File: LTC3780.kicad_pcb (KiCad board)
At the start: 2 copper layers, 46 parts, among them Q2 IPD100N04S402ATMA1, Q3 IPD100N04S402ATMA1, Q4 IPD100N04S402ATMA1, Q5 IPD100N04S402ATMA1, U1 LTC3780EGPBF

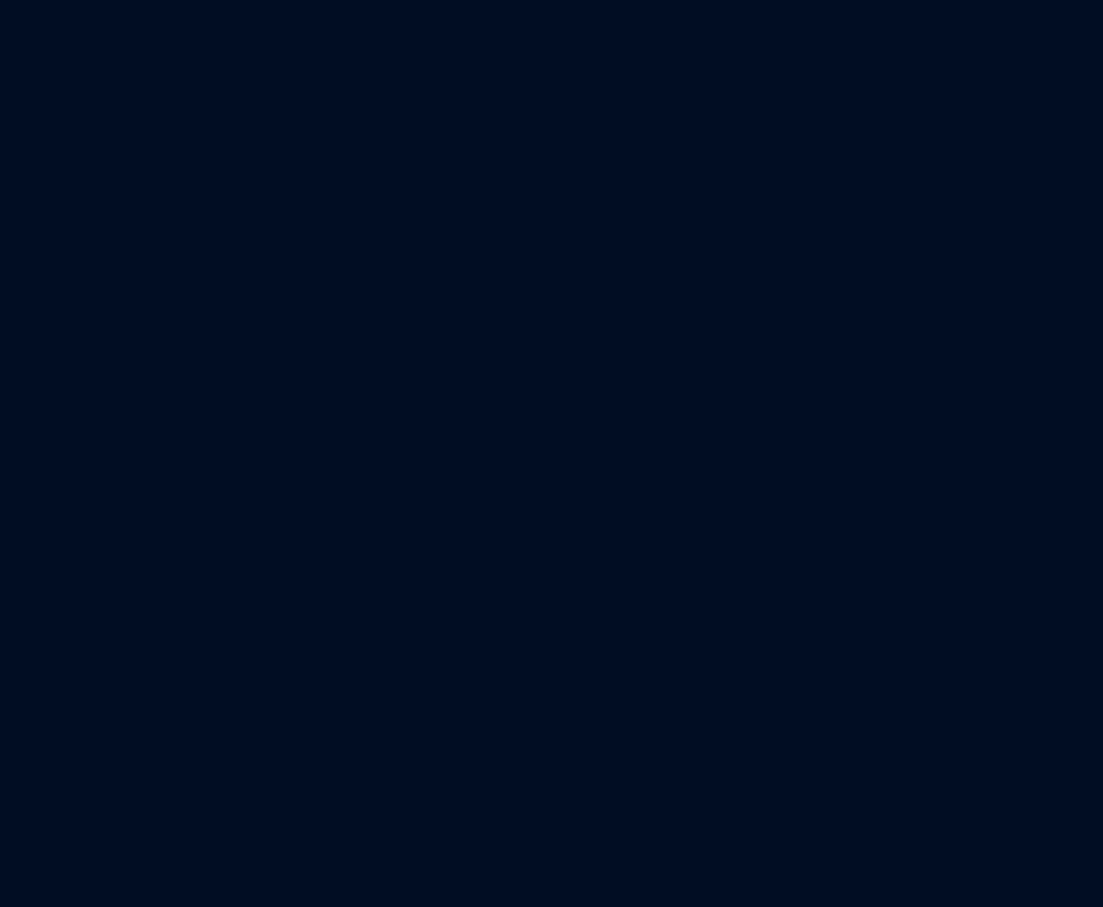
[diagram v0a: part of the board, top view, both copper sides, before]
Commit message: Updated PCB from Netlist
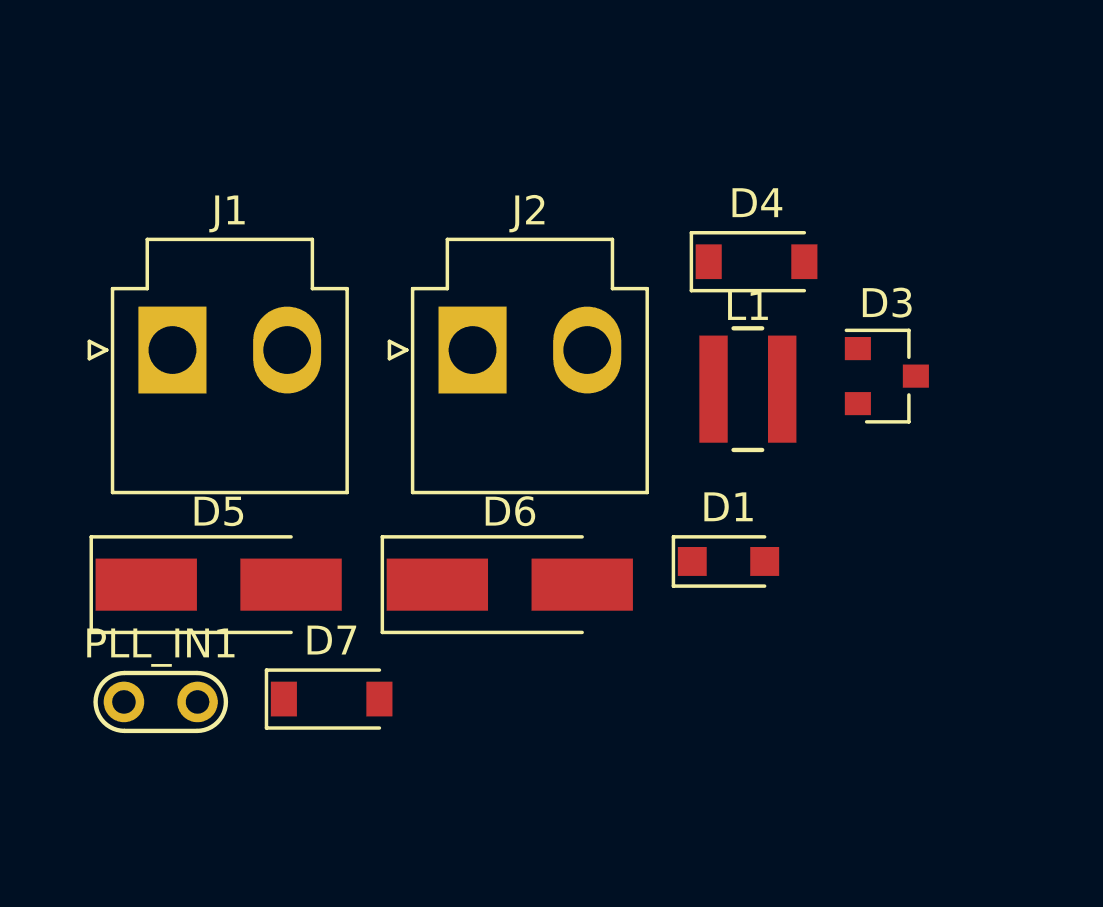
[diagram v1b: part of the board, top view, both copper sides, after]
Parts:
- added D1: 4.7V, Diodes_SMD:D_SOD-323_HandSoldering, F.Cu at (150.0, 89.3)
- added D3: 36V, Diodes_SMD:D_SOT-23_ANK, F.Cu at (155.5, 82.9)
- added D4: 1N819HW, Diodes_SMD:D_SOD-123, F.Cu at (151.0, 78.9)
- added D5: B320A, Diodes_SMD:D_SMA_Handsoldering, F.Cu at (132.4, 90.1)
- added D6: B320A, Diodes_SMD:D_SMA_Handsoldering, F.Cu at (142.5, 90.1)
- added D7: 1N819HW, Diodes_SMD:D_SOD-123, F.Cu at (136.3, 94.0)
- added J1: Screw_Terminal_01x02, Connectors_JST:JST_VH_B2P-VH_2x3.96mm_Vertical, F.Cu at (130.8, 82.0)
- added J2: Screw_Terminal_01x02, Connectors_JST:JST_VH_B2P-VH_2x3.96mm_Vertical, F.Cu at (141.2, 82.0)
- added L1: 4.7uH, Inductors:Inductor_Wurth_MAPI-4020, F.Cu at (150.7, 83.3)
- added PLL_IN1: TestPoint, Measurement_Points:Test_Point, F.Cu at (129.1, 94.1)

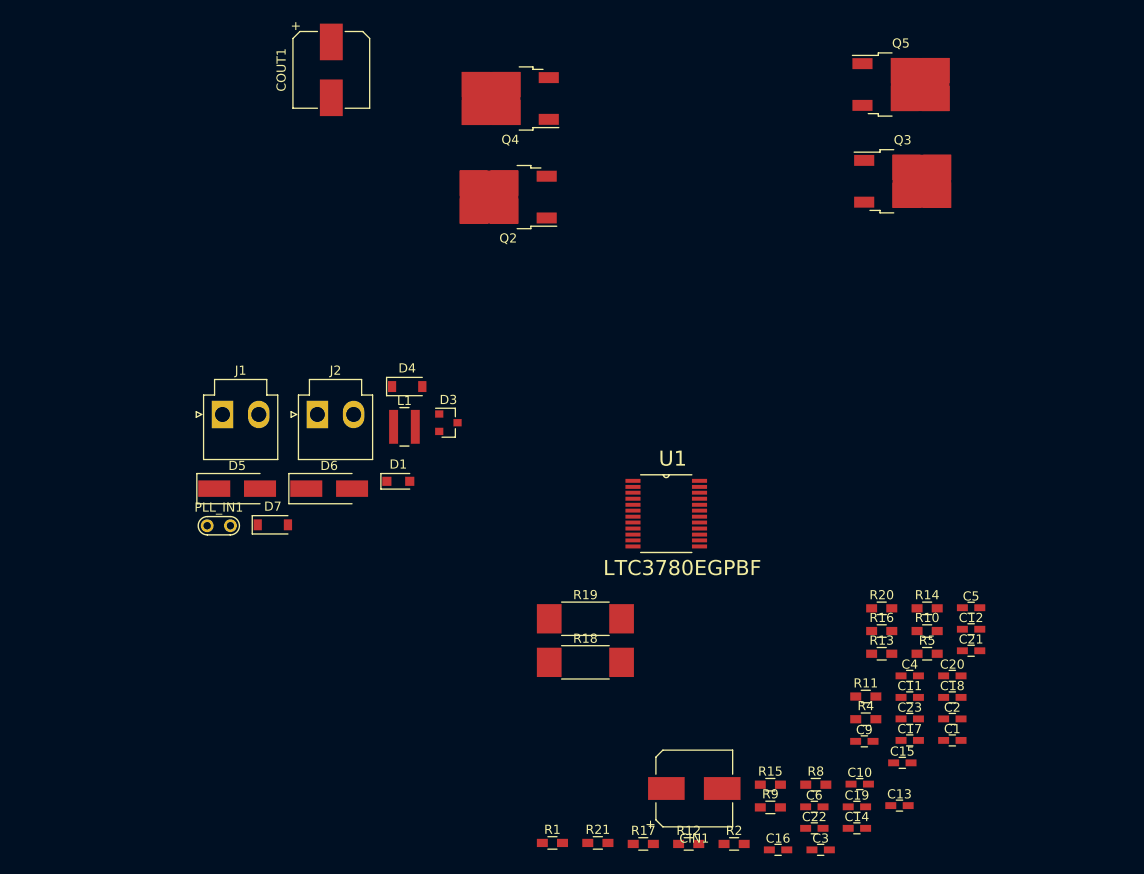
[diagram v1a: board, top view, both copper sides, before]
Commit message: Updated with drawing dimensions for board
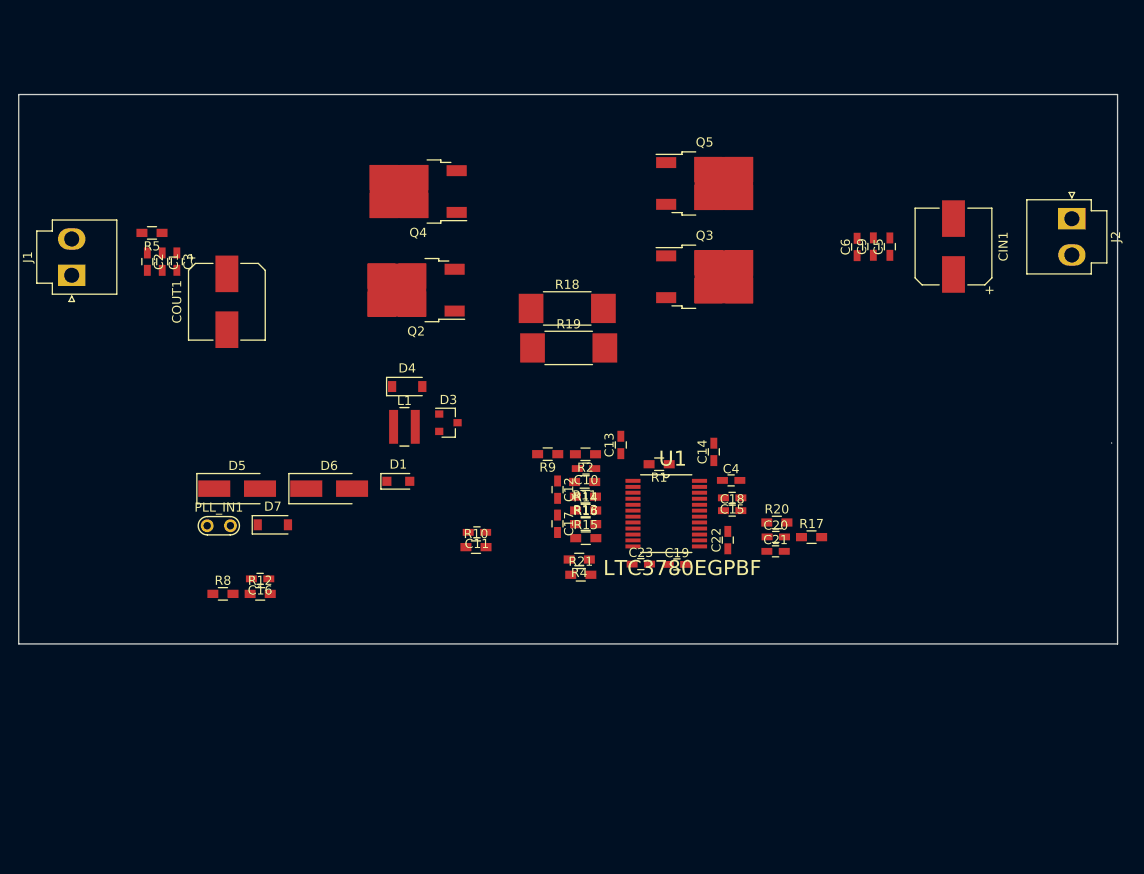
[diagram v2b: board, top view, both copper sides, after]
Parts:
- moved C2 101.1 mm to (122.6, 65.3), turned to 270 degrees
- moved C1 100.9 mm to (124.2, 65.3), turned to 270 degrees
- moved R5 96.3 mm to (123.1, 62.1), turned to 180 degrees
- moved C3 95.2 mm to (125.8, 65.3), turned to 270 degrees
- moved J2 85.1 mm to (223.6, 60.6), turned to 270 degrees
- moved R8 68.0 mm to (130.9, 101.5)
- moved CIN1 65.6 mm to (210.6, 63.6), turned to 90 degrees
- moved C16 63.8 mm to (134.9, 99.9), turned to 180 degrees
- moved C6 61.3 mm to (200.1, 63.7), turned to 90 degrees
- moved R12 54.2 mm to (134.9, 101.5)
- moved C9 54.0 mm to (201.9, 63.6), turned to 90 degrees
- moved C11 50.6 mm to (158.6, 94.8), turned to 180 degrees
- moved R10 50.1 mm to (158.5, 96.4)
- moved C13 49.8 mm to (174.3, 85.3), turned to 90 degrees
- moved C12 47.7 mm to (167.4, 90.2), turned to 270 degrees
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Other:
- board outline added: 120 x 60 mm

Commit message: Routed and placed some components
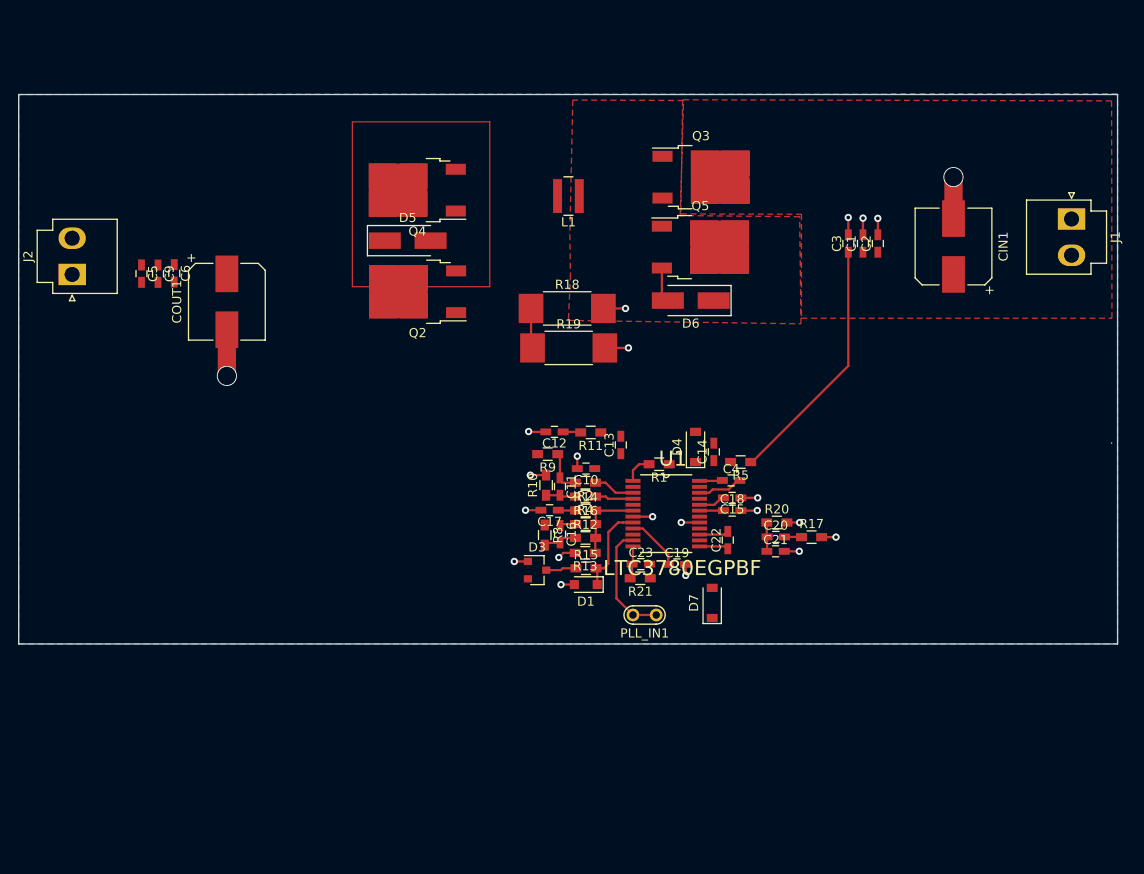
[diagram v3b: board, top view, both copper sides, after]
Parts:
- moved J1 109.4 mm to (223.5, 60.6), turned to 270 degrees
- moved J2 109.3 mm to (114.4, 66.7), turned to 90 degrees
- moved C5 81.8 mm to (122.0, 66.6), turned to 270 degrees
- moved C2 79.8 mm to (202.4, 63.3), turned to 90 degrees
- moved C9 78.2 mm to (123.8, 66.6), turned to 270 degrees
- moved C1 76.6 mm to (200.8, 63.3), turned to 90 degrees
- moved C6 74.6 mm to (125.5, 66.5), turned to 270 degrees
- moved C3 73.4 mm to (199.2, 63.3), turned to 90 degrees
- moved R5 69.0 mm to (187.4, 87.2)
- moved PLL_IN1 50.0 mm to (178.2, 103.9), turned to 180 degrees
- moved D7 48.7 mm to (184.3, 102.5), turned to 90 degrees
- moved D6 44.5 mm to (182.0, 69.5), turned to 180 degrees
- moved R12 36.0 mm to (170.5, 95.4)
- moved R8 35.7 mm to (166.0, 95.1), turned to 270 degrees
- moved C16 33.1 mm to (167.7, 95.0), turned to 270 degrees
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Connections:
- U1 pad 11: (no net) -> Net-(PLL_IN1-Pad1)
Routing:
- net GND: track 0.00 -> 45.3 mm, vias 0 -> 22
- net +VSW: track 0.00 -> 30.7 mm
- net Net-(PLL_IN1-Pad1): track 0.00 -> 12.8 mm
- net Net-(D1-Pad1): track 0.00 -> 9.95 mm
- net VSENSE: track 0.00 -> 8.71 mm
- net Net-(D6-Pad2): track 0.00 -> 8.21 mm
- net Net-(C19-Pad1): track 0.00 -> 6.14 mm
- net SW1: track 0.00 -> 4.96 mm
- net Net-(C11-Pad1): track 0.00 -> 4.74 mm
- net SENSE+: track 0.00 -> 4.55 mm
- net SENSE-: track 0.00 -> 4.19 mm
- net Net-(C16-Pad2): track 0.00 -> 3.80 mm
- net Net-(C23-Pad1): track 0.00 -> 3.60 mm
- net Net-(C11-Pad2): track 0.00 -> 3.26 mm
- net SW2: track 0.00 -> 3.23 mm
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- added copper zone on F.Cu, net +VSW
- added copper zone on B.Cu, net GND
- added copper zone on F.Cu, net SW2

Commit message: Finished PCB first layout and routing, generated gerber files
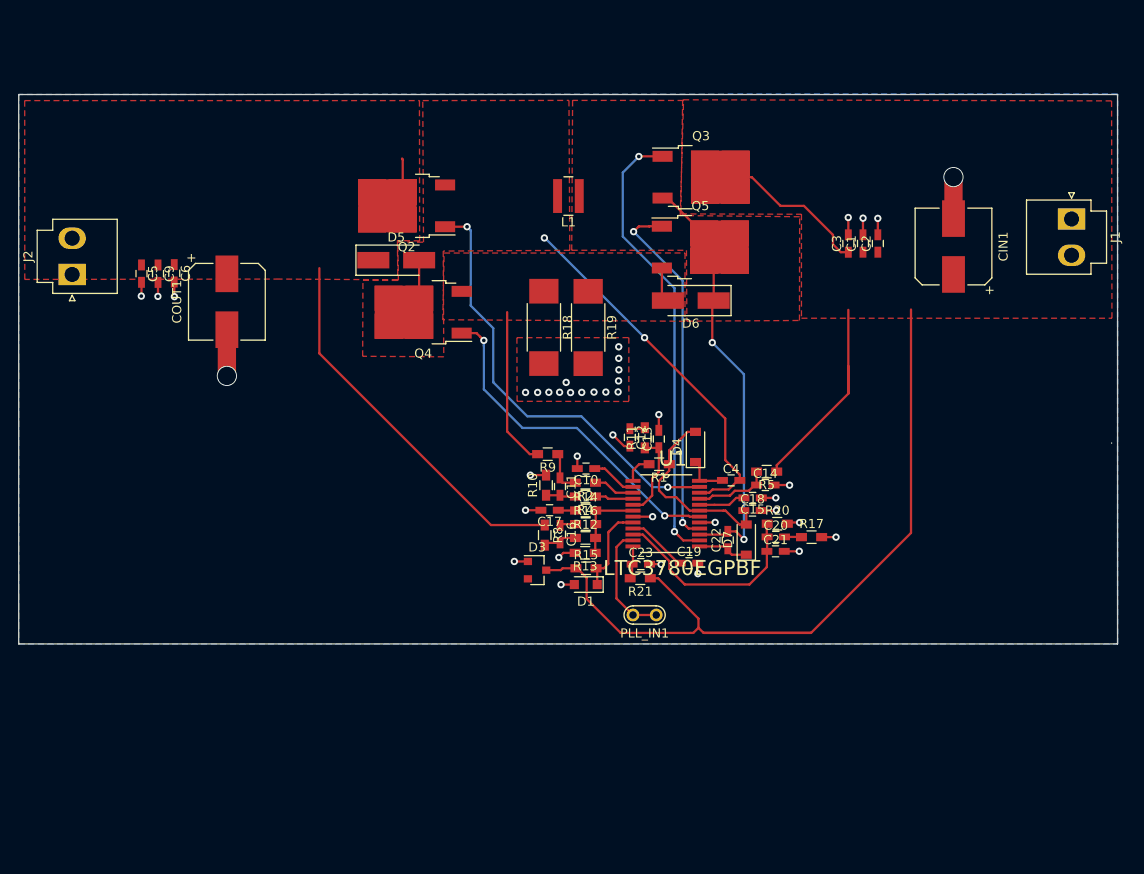
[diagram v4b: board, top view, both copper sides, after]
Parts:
- moved Q4 13.4 mm to (152.7, 70.8)
- moved Q2 9.46 mm to (150.9, 59.2)
- moved C12 8.26 mm to (175.3, 84.5), turned to 270 degrees
- moved D7 7.86 mm to (188.0, 95.6)
- moved C14 6.69 mm to (190.1, 89.7), turned to 0 degrees
- moved R11 5.93 mm to (176.9, 84.5), turned to 90 degrees
- moved C13 4.20 mm to (178.5, 84.6)
- moved R18 3.28 mm to (165.9, 72.4), turned to 270 degrees
- moved R19 3.08 mm to (170.7, 72.5), turned to 270 degrees
- moved R5 3.02 mm to (190.2, 88.2)
- moved D5 2.47 mm to (149.8, 65.1)
- moved C15 2.24 mm to (188.7, 91.1)
- moved C18 2.22 mm to (188.7, 92.5)
- moved C19 1.33 mm to (181.8, 98.2)
- moved R20 0.14 mm to (191.4, 93.9)
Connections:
- U1 pad 10: (no net) -> PLLFILTR
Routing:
- net +VSW: track 30.7 -> 135.3 mm
- net TG2: track 0.00 -> 49.8 mm, vias 0 -> 2
- net TG1: track 0.00 -> 47.9 mm, vias 0 -> 2
- net VCC: track 0.00 -> 45.4 mm
- net SW2: track 3.23 -> 46.1 mm, vias 0 -> 2
- net SW1: track 4.96 -> 46.7 mm, vias 0 -> 2
- net BG2: track 0.00 -> 39.4 mm, vias 0 -> 2
- net BG1: track 0.00 -> 37.4 mm, vias 0 -> 2
- net PLLFILTR: track 3.17 -> 23.1 mm
- net +6V: track 2.62 -> 21.2 mm
- net Net-(D6-Pad2): track 8.21 -> 21.2 mm
- net Net-(C13-Pad1): track 0.00 -> 9.58 mm
- net Net-(C14-Pad1): track 0.00 -> 8.33 mm
- net Net-(C10-Pad1): track 0.00 -> 5.01 mm
- net GND: track 45.3 -> 49.4 mm, vias 22 -> 40
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- added copper zone on F.Cu, net GND
- added copper zone on F.Cu, net Net-(D6-Pad2)
- added copper zone on F.Cu, net SW1
- added copper zone on F.Cu, net VCC
